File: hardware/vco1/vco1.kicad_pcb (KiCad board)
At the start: 2 copper layers, 50 x 100 mm, 77 parts, among them J1 AudioJack2_SwitchT, J10 Conn_01x02_Pin, J2 AudioJack2_SwitchT, J3 AudioJack2_SwitchT, J4 AudioJack2_SwitchT, J5 Conn_02x08_Odd_Even, J6 AudioJack2_SwitchT, J7 AudioJack2_SwitchT, J8 Conn_01x02_Pin, J9 Conn_01x02_Pin, Q1 2N3904, Q2 2N3906, U1 40106, U2 TL074, U3 TL074

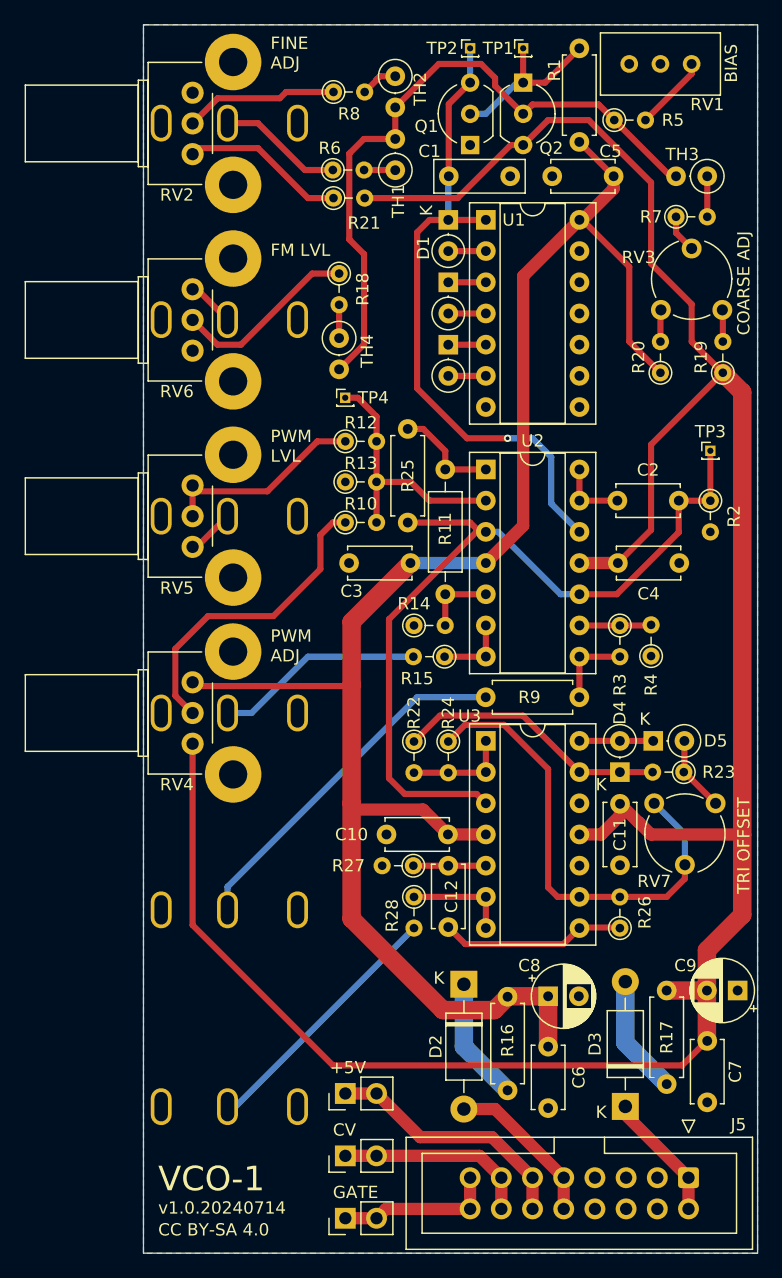
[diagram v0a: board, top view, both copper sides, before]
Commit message: added more test points and documentation. Currently cannot adjust to f_osc < 800Hz
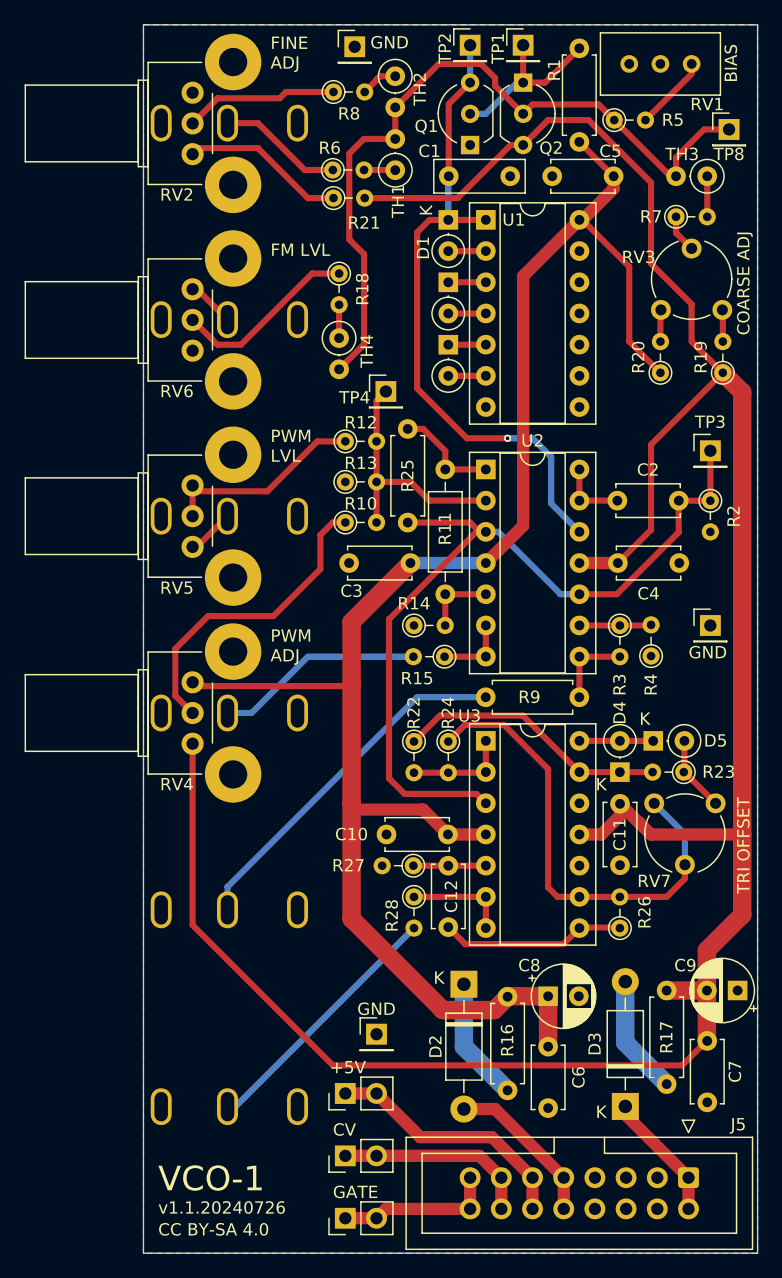
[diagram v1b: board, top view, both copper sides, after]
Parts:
- added TP5: TestPoint, Connector_PinHeader_2.54mm:PinHeader_1x01_P2.54mm_Vertical, F.Cu at (187.2, 41.8)
- added TP6: TestPoint, Connector_PinHeader_2.54mm:PinHeader_1x01_P2.54mm_Vertical, F.Cu at (216.2, 88.9)
- added TP7: TestPoint, Connector_PinHeader_2.54mm:PinHeader_1x01_P2.54mm_Vertical, F.Cu at (189.0, 122.2)
- added TP8: TestPoint, Connector_PinHeader_2.54mm:PinHeader_1x01_P2.54mm_Vertical, F.Cu at (217.7, 48.5)
- TP1, TP2, TP3, TP4: footprint Connector_PinHeader_1.00mm:PinHeader_1x01_P1.00mm_Vertical -> Connector_PinHeader_2.54mm:PinHeader_1x01_P2.54mm_Vertical
- moved TP4 3.35 mm to (189.7, 69.8)
- moved TP1 0.25 mm to (200.9, 41.7)
- moved TP2 0.25 mm to (196.6, 41.7)
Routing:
- net /VIN: track 54.8 -> 61.6 mm
- net Net-(U2A--): track 21.3 -> 20.5 mm
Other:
- board text added: "GND"
- board text added: "v1.1.20240726"
- board text removed: "v1.0.20240714"

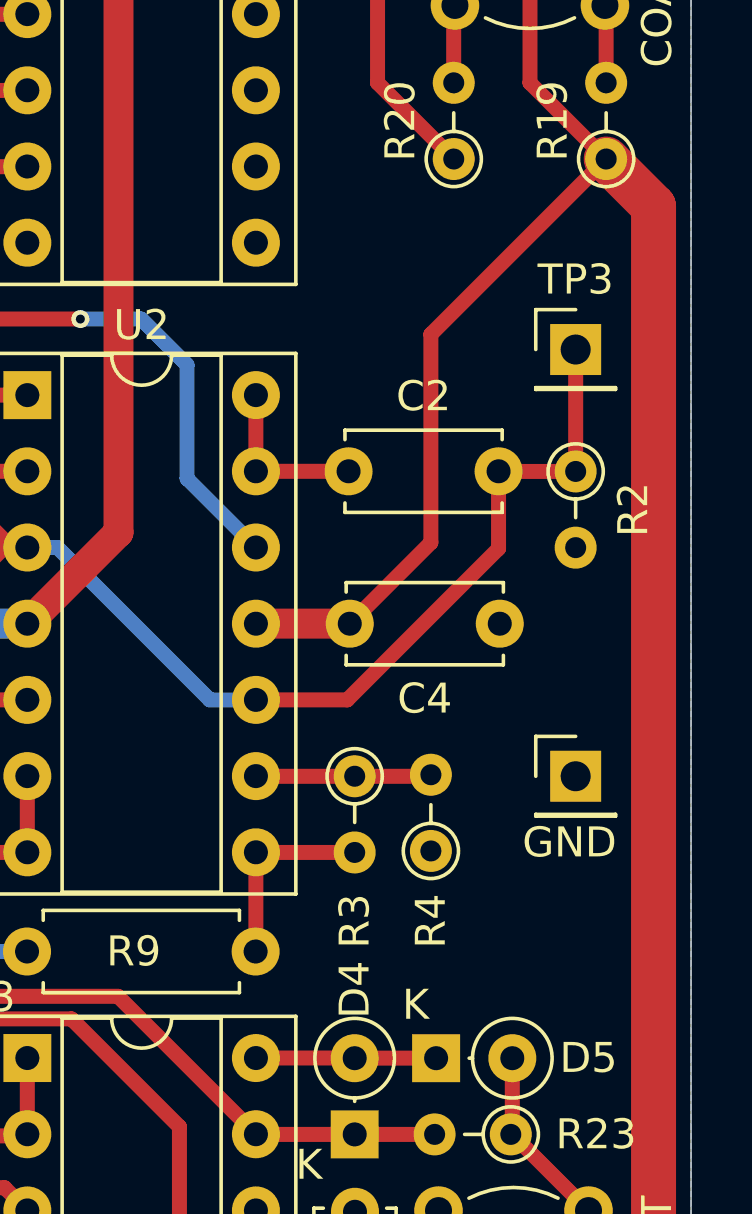
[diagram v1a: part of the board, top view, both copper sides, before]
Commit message: Update schematic and board to v1.1 based on initial test from v1 PCB. Changes in README.md
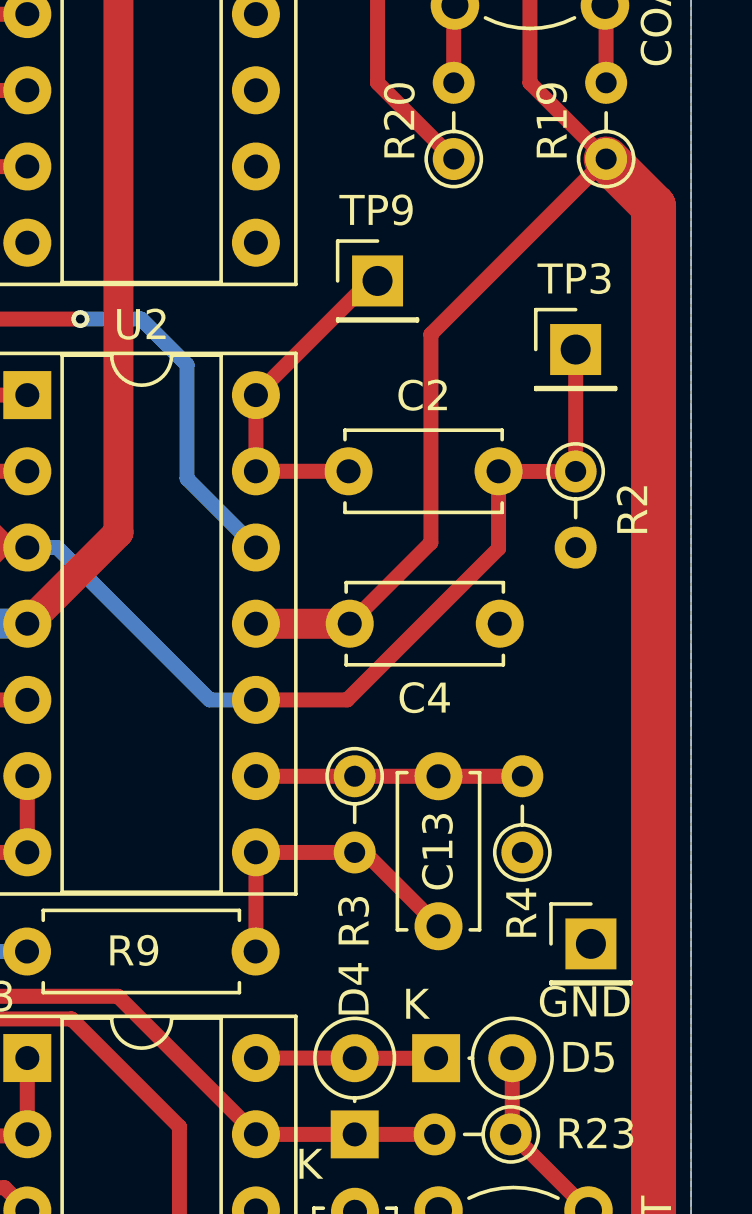
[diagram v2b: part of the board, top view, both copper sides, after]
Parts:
- added C13: 22p, Capacitor_THT:C_Disc_D5.0mm_W2.5mm_P5.00mm, F.Cu at (211.6, 88.9)
- added TP9: TestPoint, Connector_PinHeader_2.54mm:PinHeader_1x01_P2.54mm_Vertical, F.Cu at (209.6, 72.4)
- R14: value 68k -> 82k
- R26: value 22k -> 68k
- moved TP6 5.61 mm to (216.7, 94.5)
- moved R4 3.05 mm to (214.4, 91.4)
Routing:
- net Net-(U2D--): track 5.63 -> 11.3 mm
- net Net-(C13-Pad2): track 6.61 -> 10.4 mm
- net Net-(U2C--): track 5.85 -> 8.88 mm
